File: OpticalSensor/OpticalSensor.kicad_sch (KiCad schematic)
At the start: 4 parts, among them J1 Conn_01x03, U1 EE_SX1103

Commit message: Initial board
Added complementary components
Board should be functional
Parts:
- removed J1: Conn_01x03, Connector_JST:JST_SH_SM03B-SRSS-TB_1x03-1MP_P1.00mm_Horizontal, symbol Connector_Generic:Conn_01x03
- added D1: BAT54KFILM, Diode_SMD:D_SOD-523, symbol Device:D_Schottky
- added J1: Conn_01x03_MountingPin, Connector_JST:JST_SH_SM03B-SRSS-TB_1x03-1MP_P1.00mm_Horizontal, symbol Connector_Generic_MountingPin:Conn_01x03_MountingPin
- added Q1: T2N7002AK, Package_TO_SOT_SMD:SOT-23, symbol Transistor_FET:T2N7002AK
- added R1: 330R, Resistor_SMD:R_0402_1005Metric, symbol Device:R
- added R2, R4: 10K, Resistor_SMD:R_0402_1005Metric, symbol Device:R
- added R3: 56K, Resistor_SMD:R_0402_1005Metric, symbol Device:R
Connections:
- net GND: now also U1.2, U1.3, D1.2 (A), Q1.2 (S)
- net at U1.1: now also R1.2
- net at U1.4: now also Q1.1 (G), R2.2
- new net: D1.1 (K), J1.1 (Pin_1), R3.1
- new net OUT: J1.3 (Pin_3), Q1.3 (D), R3.2, R4.1
- new net VCC: J1.2 (Pin_2), R1.1, R2.1, R4.2
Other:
- moved on the sheet: H1, H2, U1

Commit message: Power and status led
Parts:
- added D2: LED_Dual_AKAK, easyeda2kicad:LED-ARRAY-SMD_4P-L1.6-W1.3-BR-FD, symbol Device:LED_Dual_AKAK
- added R5, R6: 120R, Resistor_SMD:R_0402_1005Metric, symbol Device:R
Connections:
- net GND: now also D2.2 (K1), D2.4 (K2)
- net OUT: now also R5.1
- net VCC: now also R6.1
- new net: D2.3 (A2), R6.2
- new net: D2.1 (A1), R5.2

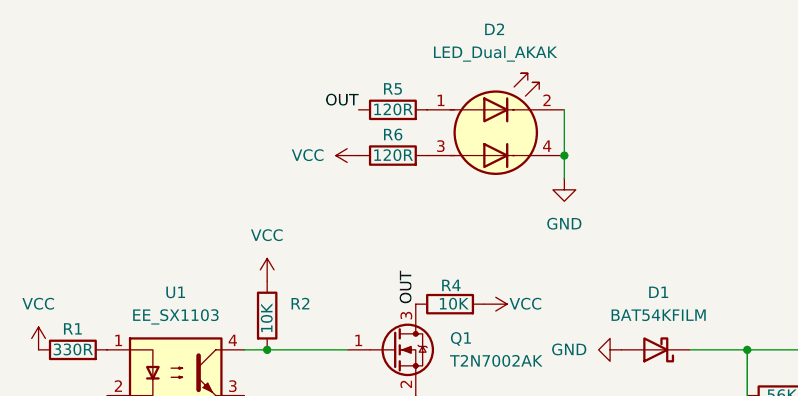
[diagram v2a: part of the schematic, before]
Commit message: LCSC component part numbers, board resize
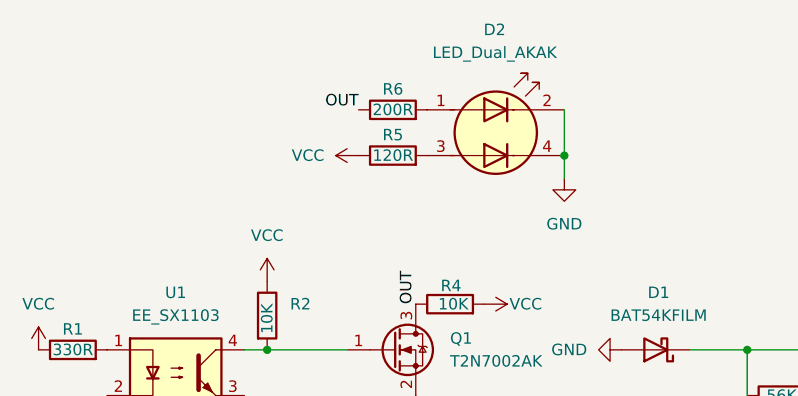
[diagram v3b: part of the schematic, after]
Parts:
- D1: LCSC (none) -> C283259
- D2: LCSC (none) -> C131286
- J1: LCSC (none) -> C160403
- Q1: LCSC (none) -> C5224226
- R1: LCSC (none) -> C2759496
- R2, R4: LCSC (none) -> C414854
- R3: LCSC (none) -> C131604
- R5: LCSC (none) -> C159875
- R6: value 120R -> 200R; LCSC (none) -> C2759465
- U1: LCSC (none) -> C2931100
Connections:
- net OUT: now also R6.1; no longer R5.1
- net VCC: now also R5.1; no longer R6.1
- net at R6.2: now also D2.1 (A1); no longer D2.3 (A2)
- net at R5.2: now also D2.3 (A2); no longer D2.1 (A1)
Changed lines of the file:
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@@
+			)
+		)
+		(property "LCSC" " C414854"
+			(at 147.32 99.06 0)
+			(effects
+				(font
+					(size 1.27 1.27)
+				)
+				(hide yes)
 			)
 		)
@@
 				(path "/c3d09ac2-1481-485c-bab2-9a255faeb2fa"
 					(reference "R2")
-					(unit 1)
-				)
-			)
-		)
-	)
-	(symbol
-		(lib_id "Device:R")
-		(at 161.29 81.28 90)
-		(unit 1)
-		(exclude_from_sim no)
-		(in_bom yes)
-		(on_board yes)
-		(dnp no)
-		(property "Reference" "R6"
-			(at 161.29 78.994 90)
-			(effects
-				(font
-					(size 1.27 1.27)
-				)
-			)
-		)
-		(property "Value" "120R"
-			(at 161.29 81.28 90)
-			(effects
-				(font
-					(size 1.27 1.27)
-				)
-			)
-		)
-		(property "Footprint" "Resistor_SMD:R_0402_1005Metric"
-			(at 161.29 83.058 90)
-			(effects
-				(font
-					(size 1.27 1.27)
-				)
-				(hide yes)
-			)
-		)
-		(property "Datasheet" "~"
-			(at 161.29 81.28 0)
-			(effects
-				(font
-					(size 1.27 1.27)
-				)
-				(hide yes)
-			)
-		)
-		(property "Description" "Resistor"
-			(at 161.29 81.28 0)
-			(effects
-				(font
-					(size 1.27 1.27)
-				)
-				(hide yes)
-			)
-		)
-		(pin "1"
-		)
-		(pin "2"
-		)
-		(instances
-			(project "OpticalSensor"
-				(path "/c3d09ac2-1481-485c-bab2-9a255faeb2fa"
-					(reference "R6")
 					(unit 1)
 				)
@@
 			)
 		)
+		(property "LCSC" "C283259"
+			(at 190.5 102.87 0)
+			(effects
+				(font
+					(size 1.27 1.27)
+				)
+				(hide yes)
+			)
+		)
 		(pin "1"
 		)
@@
 			)
 		)
+		(property "LCSC" "C160403"
+			(at 222.25 105.41 0)
+			(effects
+				(font
+					(size 1.27 1.27)
+				)
+				(hide yes)
+			)
+		)
 		(pin "2"
 		)
@@
 			)
 		)
+		(property "LCSC" "C5224226"
+			(at 161.29 102.87 0)
+			(effects
+				(font
+					(size 1.27 1.27)
+				)
+				(hide yes)
+			)
+		)
 		(pin "1"
 		)
@@
 	)
 	(symbol
+		(lib_id "Device:R")
+		(at 161.29 76.2 90)
+		(unit 1)
+		(exclude_from_sim no)
+		(in_bom yes)
+		(on_board yes)
+		(dnp no)
+		(property "Reference" "R6"
+			(at 161.29 73.914 90)
+			(effects
+				(font
+					(size 1.27 1.27)
+				)
+			)
+		)
+		(property "Value" "200R"
+			(at 161.29 76.2 90)
+			(effects
+				(font
+					(size 1.27 1.27)
+				)
+			)
+		)
+		(property "Footprint" "Resistor_SMD:R_0402_1005Metric"
+			(at 161.29 77.978 90)
+			(effects
+				(font
+					(size 1.27 1.27)
+				)
+				(hide yes)
+			)
+		)
+		(property "Datasheet" "~"
+			(at 161.29 76.2 0)
+			(effects
+				(font
+					(size 1.27 1.27)
+				)
+				(hide yes)
+			)
+		)
+		(property "Description" "Resistor"
+			(at 161.29 76.2 0)
+			(effects
+				(font
+					(size 1.27 1.27)
+				)
+				(hide yes)
+			)
+		)
+		(property "LCSC" " C2759465"
+			(at 161.29 76.2 90)
+			(effects
+				(font
+					(size 1.27 1.27)
+				)
+				(hide yes)
+			)
+		)
+		(pin "1"
+		)
+		(pin "2"
+		)
+		(instances
+			(project "OpticalSensor"
+				(path "/c3d09ac2-1481-485c-bab2-9a255faeb2fa"
+					(reference "R6")
+					(unit 1)
+				)
+			)
+		)
+	)
+	(symbol
 		(lib_id "Device:LED_Dual_AKAK")
 		(at 172.72 78.74 0)
@@
 			)
 		)
+		(property "LCSC" "C131286"
+			(at 172.72 78.74 0)
+			(effects
+				(font
+					(size 1.27 1.27)
+				)
+				(hide yes)
+			)
+		)
 		(pin "4"
 		)
@@
 			)
 		)
+		(property "LCSC" " C2759496"
+			(at 125.73 102.87 90)
+			(effects
+				(font
+					(size 1.27 1.27)
+				)
+				(hide yes)
+			)
+		)
 		(pin "1"
 		)
@@
 	(symbol
 		(lib_id "Device:R")
-		(at 161.29 76.2 90)
-		(unit 1)
-		(exclude_from_sim no)
-		(in_bom yes)
-		(on_board yes)
-		(dnp no)
-		(property "Reference" "R5"
-			(at 161.29 73.914 90)
-			(effects
-				(font
-					(size 1.27 1.27)
-				)
-			)
-		)
-		(property "Value" "120R"
-			(at 161.29 76.2 90)
-			(effects
-				(font
-					(size 1.27 1.27)
-				)
-			)
-		)
-		(property "Footprint" "Resistor_SMD:R_0402_1005Metric"
-			(at 161.29 77.978 90)
-			(effects
-				(font
-					(size 1.27 1.27)
-				)
-				(hide yes)
-			)
-		)
-		(property "Datasheet" "~"
-			(at 161.29 76.2 0)
-			(effects
-				(font
-					(size 1.27 1.27)
-				)
-				(hide yes)
-			)
-		)
-		(property "Description" "Resistor"
-			(at 161.29 76.2 0)
-			(effects
-				(font
-					(size 1.27 1.27)
-				)
-				(hide yes)
-			)
-		)
-		(pin "1"
-		)
-		(pin "2"
-		)
-		(instances
-			(project "OpticalSensor"
-				(path "/c3d09ac2-1481-485c-bab2-9a255faeb2fa"
-					(reference "R5")
-					(unit 1)
-				)
-			)
-		)
-	)
-	(symbol
-		(lib_id "Device:R")
 		(at 167.64 97.79 90)
 		(unit 1)
@@
 		(property "Description" "Resistor"
 			(at 167.64 97.79 0)
+			(effects
+				(font
+					(size 1.27 1.27)
+				)
+				(hide yes)
+			)
+		)
+		(property "LCSC" " C414854"
+			(at 167.64 97.79 90)
 			(effects
 				(font
@@
 			)
 		)
+		(property "LCSC" "C2931100"
+			(at 137.16 105.41 0)
+			(effects
+				(font
+					(size 1.27 1.27)
+				)
+				(hide yes)
+			)
+		)
 		(pin "4"
 		)
@@
 			)
 		)
+		(property "LCSC" " C131604"
+			(at 204.47 107.95 90)
+			(effects
+				(font
+					(size 1.27 1.27)
+				)
+				(hide yes)
+			)
+		)
 		(pin "2"
 		)
@@
 					(unit 1)
 				)
+			)
+		)
+	)
+	(symbol
+		(lib_id "Device:R")
+		(at 161.29 81.28 90)
+		(unit 1)
+		(exclude_from_sim no)
+		(in_bom yes)
+		(on_board yes)
+		(dnp no)
+		(property "Reference" "R5"
+			(at 161.29 78.994 90)
+			(effects
+				(font
+					(size 1.27 1.27)
+				)
+			)
+		)
+		(property "Value" "120R"
+			(at 161.29 81.28 90)
+			(effects
+				(font
+					(size 1.27 1.27)
+				)
+			)
+		)
+		(property "Footprint" "Resistor_SMD:R_0402_1005Metric"
+			(at 161.29 83.058 90)
+			(effects
+				(font
+					(size 1.27 1.27)
+				)
+				(hide yes)
+			)
+		)
+		(property "Datasheet" "~"
+			(at 161.29 81.28 0)
+			(effects
+				(font
+					(size 1.27 1.27)
+				)
+				(hide yes)
+			)
+		)
+		(property "Description" "Resistor"
+			(at 161.29 81.28 0)
+			(effects
+				(font
+					(size 1.27 1.27)
+				)
+				(hide yes)
+			)
+		)
+		(property "LCSC" "C159875"
+			(at 161.29 81.28 90)
+			(effects
+				(font
+					(size 1.27 1.27)
+				)
+				(hide yes)
+			)
+		)
+		(pin "1"
+		)
+		(pin "2"
+		)
+		(instances
+			(project "OpticalSensor"
+				(path "/c3d09ac2-1481-485c-bab2-9a255faeb2fa"
+					(reference "R5")
+					(unit 1)
+				)

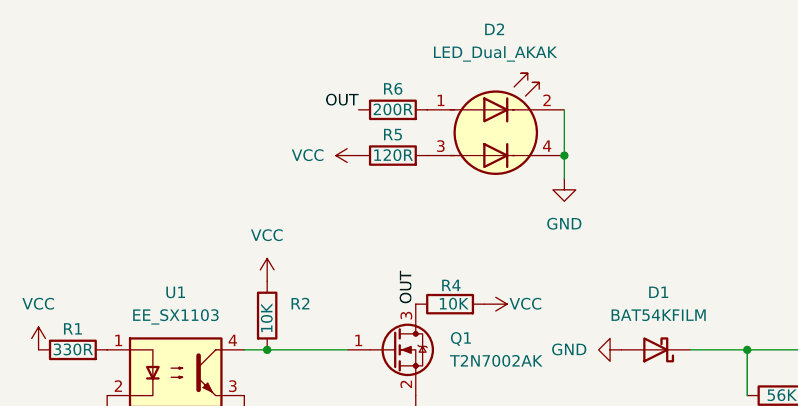
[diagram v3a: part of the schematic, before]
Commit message: Led footprint updates
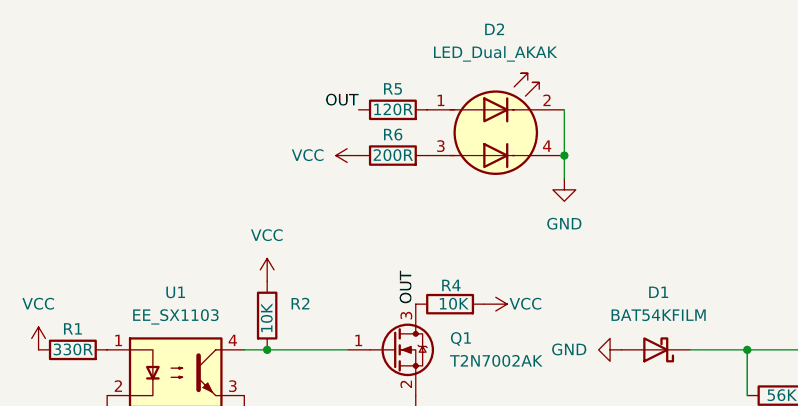
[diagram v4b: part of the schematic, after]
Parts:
- D2: footprint easyeda2kicad:LED-ARRAY-SMD_4P-L1.6-W1.3-BR-FD -> Lighting:QBLP600-RIB
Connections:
- net OUT: now also R5.1; no longer R6.1
- net VCC: now also R6.1; no longer R5.1
- net at R6.2: now also D2.3 (A2); no longer D2.1 (A1)
- net at R5.2: now also D2.1 (A1); no longer D2.3 (A2)
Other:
- moved on the sheet: R5, R6
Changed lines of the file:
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@@
 	(symbol
 		(lib_id "Device:R")
-		(at 161.29 76.2 90)
+		(at 161.29 81.28 90)
 		(unit 1)
 		(exclude_from_sim no)
@@
 		(dnp no)
 		(property "Reference" "R6"
-			(at 161.29 73.914 90)
+			(at 161.29 78.994 90)
 			(effects
 				(font
@@
 		)
 		(property "Value" "200R"
-			(at 161.29 76.2 90)
+			(at 161.29 81.28 90)
 			(effects
 				(font
@@
 		)
 		(property "Footprint" "Resistor_SMD:R_0402_1005Metric"
-			(at 161.29 77.978 90)
+			(at 161.29 83.058 90)
 			(effects
 				(font
@@
 		)
 		(property "Datasheet" "~"
-			(at 161.29 76.2 0)
+			(at 161.29 81.28 0)
 			(effects
 				(font
@@
 		)
 		(property "Description" "Resistor"
-			(at 161.29 76.2 0)
+			(at 161.29 81.28 0)
 			(effects
 				(font
@@
 		)
 		(property "LCSC" " C2759465"
-			(at 161.29 76.2 90)
+			(at 161.29 81.28 90)
 			(effects
 				(font
@@
 			)
 		)
-		(property "Footprint" "easyeda2kicad:LED-ARRAY-SMD_4P-L1.6-W1.3-BR-FD"
+		(property "Footprint" "Lighting:QBLP600-RIB"
 			(at 173.482 78.74 0)
 			(effects
@@
 	(symbol
 		(lib_id "Device:R")
-		(at 161.29 81.28 90)
+		(at 161.29 76.2 90)
 		(unit 1)
 		(exclude_from_sim no)
@@
 		(dnp no)
 		(property "Reference" "R5"
-			(at 161.29 78.994 90)
+			(at 161.29 73.914 90)
 			(effects
 				(font
@@
 		)
 		(property "Value" "120R"
-			(at 161.29 81.28 90)
+			(at 161.29 76.2 90)
 			(effects
 				(font
@@
 		)
 		(property "Footprint" "Resistor_SMD:R_0402_1005Metric"
-			(at 161.29 83.058 90)
+			(at 161.29 77.978 90)
 			(effects
 				(font
@@
 		)
 		(property "Datasheet" "~"
-			(at 161.29 81.28 0)
+			(at 161.29 76.2 0)
 			(effects
 				(font
@@
 		)
 		(property "Description" "Resistor"
-			(at 161.29 81.28 0)
+			(at 161.29 76.2 0)
 			(effects
 				(font
@@
 		)
 		(property "LCSC" "C159875"
-			(at 161.29 81.28 90)
-			(effects
-				(font
+			(at 161.29 76.2 90)
+			(effects
+				(font

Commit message: Remove incompatible lcsc id
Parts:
- D2: LCSC C131286 -> (none)
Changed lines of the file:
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@@
-			)
-		)
-		(property "LCSC" "C131286"
-			(at 172.72 78.74 0)
-			(effects
-				(font
-					(size 1.27 1.27)
-				)
-				(hide yes)
 			)
 		)

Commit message: DigiKey Part references
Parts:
- D1: Part (none) -> BAT54KFILM
- D2: Part (none) -> QBLP600-RIB
- J1: Part (none) -> SM03B-SRSS-TB
- Q1: Part (none) -> T2N7002AK,LM
- R1: Part (none) -> ERJ-2RKF3300X
- R2, R4: Part (none) -> ERJ-2RKF1002X
- R3: Part (none) -> ERJ-2RKF5602X
- R5: Partq (none) -> ERJ-2RKF1200X
- R6: Part (none) -> ERJ-2RKF2000X
- U1: Part (none) -> EE-SX1103
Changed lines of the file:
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@@
+			)
+		)
+		(property "Part" "ERJ-2RKF1002X"
+			(at 147.32 99.06 0)
+			(effects
+				(font
+					(size 1.27 1.27)
+				)
+				(hide yes)
 			)
 		)
@@
 			)
 		)
+		(property "Part" "BAT54KFILM"
+			(at 190.5 102.87 0)
+			(effects
+				(font
+					(size 1.27 1.27)
+				)
+				(hide yes)
+			)
+		)
 		(pin "1"
 		)
@@
 			)
 		)
+		(property "Part" "SM03B-SRSS-TB"
+			(at 222.25 105.41 0)
+			(effects
+				(font
+					(size 1.27 1.27)
+				)
+				(hide yes)
+			)
+		)
 		(pin "2"
 		)
@@
 			)
 		)
+		(property "Part" "T2N7002AK,LM"
+			(at 161.29 102.87 0)
+			(effects
+				(font
+					(size 1.27 1.27)
+				)
+				(hide yes)
+			)
+		)
 		(pin "1"
 		)
@@
 			)
 		)
+		(property "Part" "ERJ-2RKF2000X"
+			(at 161.29 81.28 90)
+			(effects
+				(font
+					(size 1.27 1.27)
+				)
+				(hide yes)
+			)
+		)
 		(pin "1"
 		)
@@
 			)
 		)
+		(property "Part" "QBLP600-RIB"
+			(at 172.72 78.74 0)
+			(effects
+				(font
+					(size 1.27 1.27)
+				)
+				(hide yes)
+			)
+		)
 		(pin "4"
 		)
@@
 			)
 		)
+		(property "Part" "ERJ-2RKF3300X"
+			(at 125.73 102.87 90)
+			(effects
+				(font
+					(size 1.27 1.27)
+				)
+				(hide yes)
+			)
+		)
 		(pin "1"
 		)
@@
 			)
 		)
+		(property "Part" "ERJ-2RKF1002X"
+			(at 167.64 97.79 90)
+			(effects
+				(font
+					(size 1.27 1.27)
+				)
+				(hide yes)
+			)
+		)
 		(pin "1"
 		)
@@
 			)
 		)
+		(property "Part" "EE-SX1103"
+			(at 137.16 105.41 0)
+			(effects
+				(font
+					(size 1.27 1.27)
+				)
+				(hide yes)
+			)
+		)
 		(pin "4"
 		)
@@
 			)
 		)
+		(property "Part" "ERJ-2RKF5602X"
+			(at 204.47 107.95 90)
+			(effects
+				(font
+					(size 1.27 1.27)
+				)
+				(hide yes)
+			)
+		)
 		(pin "2"
 		)
@@
 			(at 161.29 76.2 90)
 			(effects
+				(font
+					(size 1.27 1.27)
+				)
+				(hide yes)
+			)
+		)
+		(property "Partq" "ERJ-2RKF1200X"
+			(at 161.29 76.2 90)
+			(effects

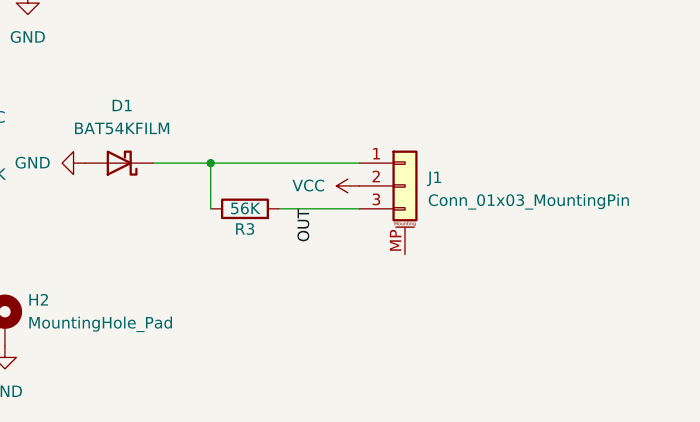
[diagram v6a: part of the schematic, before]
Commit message: fix optical sensor routing
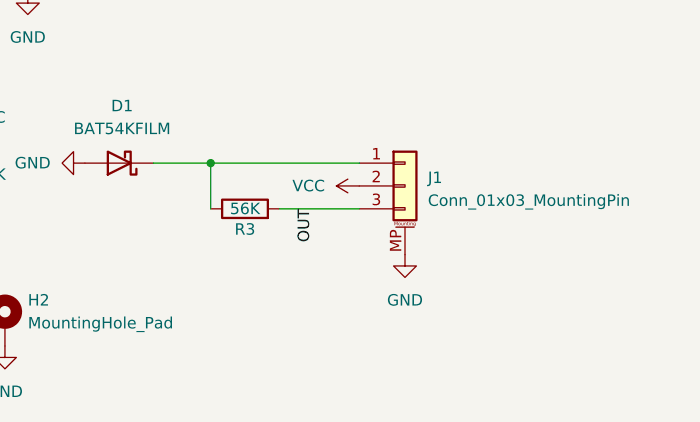
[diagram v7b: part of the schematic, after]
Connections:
- net GND: now also J1.MP (MountPin)
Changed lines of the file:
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@@
+	(symbol
+		(lib_id "power:GND")
+		(at 222.25 113.03 0)
+		(unit 1)
+		(exclude_from_sim no)
+		(in_bom yes)
+		(on_board yes)
+		(dnp no)
+		(fields_autoplaced yes)
+		(property "Reference" "#PWR013"
+			(at 222.25 119.38 0)
+			(effects
+				(font
+					(size 1.27 1.27)
+				)
+				(hide yes)
+			)
+		)
+		(property "Value" "GND"
+			(at 222.25 118.11 0)
+			(effects
+				(font
+					(size 1.27 1.27)
+				)
+			)
+		)
+		(property "Footprint" ""
+			(at 222.25 113.03 0)
+			(effects
+				(font
+					(size 1.27 1.27)
+				)
+				(hide yes)
+			)
+		)
+		(property "Datasheet" ""
+			(at 222.25 113.03 0)
+			(effects
+				(font
+					(size 1.27 1.27)
+				)
+				(hide yes)
+			)
+		)
+		(property "Description" "Power symbol creates a global label with name \"GND\" , ground"
+			(at 222.25 113.03 0)
+			(effects
+				(font
+					(size 1.27 1.27)
+				)
+				(hide yes)
+			)
+		)
+		(pin "1"
+		)
+		(instances
+			(project "OpticalSensor"
+				(path "/c3d09ac2-1481-485c-bab2-9a255faeb2fa"
+					(reference "#PWR013")
+					(unit 1)
+				)
+			)
+		)
+	)
 	(symbol
 		(lib_id "power:GND")
